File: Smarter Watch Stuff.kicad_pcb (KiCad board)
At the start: 2 copper layers, 39.5 x 39.5 mm, 63 parts, among them J3 CX70M-24P1, M1 Motor_DC, Q1 2N7002, Q2 2N7002, Q3 2N7002, Q4 2N7002, SW1 SW_SPST, SW2 SW_SPST, U1 MCP7940N-xSN, U10 MAX30102, U11 BMI160, U12 M24C64-WMN6TP, U2 TSL25911FN, U3 MCP73831-2-MC, U4 TCR2EE10, U5 ESP32-C6-MINI-1, U6 SHTC3, U7 TMP117xxDRV, U9 MIC5365-1.8YC5, Y1 Crystal

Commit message: Layout start
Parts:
- added C15: 1nF, Capacitor_SMD:C_0603_1608Metric, F.Cu at (100.5, 83.4)
- added C16: 4.7uF, Capacitor_SMD:C_0402_1005Metric, F.Cu at (106.9, 83.2)
- added C17: 100pF, Capacitor_SMD:C_0603_1608Metric, F.Cu at (100.5, 86.0)
- added C18: 2.2uF, Capacitor_SMD:C_0603_1608Metric, F.Cu at (100.5, 88.5)
- added C19: 100pF, Capacitor_SMD:C_0603_1608Metric, F.Cu at (100.5, 91.0)
- added R21: 470R, Resistor_SMD:R_0402_1005Metric, F.Cu at (104.0, 83.2)
- added R22: 470R, Resistor_SMD:R_0402_1005Metric, F.Cu at (104.0, 85.2)
- added R23: 470R, Resistor_SMD:R_0402_1005Metric, F.Cu at (104.0, 87.2)
- added U13: ~, Package_DFN_QFN:DFN-12-1EP_3x3mm_P0.5mm_EP1.6x2.5mm, F.Cu at (49.1, 79.1)
- SW1, SW2: moved to B.Cu
- moved U11 111.5 mm to (49.8, 71.2), turned to 180 degrees
- moved C14 103.9 mm to (54.0, 68.0)
- moved Y1 101.6 mm to (35.0, 70.5), turned to 90 degrees
- moved U1 97.0 mm to (41.0, 71.0)
- moved U12 96.8 mm to (45.0, 90.5)
- moved J6 96.7 mm to (39.0, 90.5)
- moved J5 95.8 mm to (36.5, 90.5)
- moved J4 94.8 mm to (34.0, 90.5)
- moved J2 79.4 mm to (51.0, 90.5)
- moved J1 74.1 mm to (53.5, 90.5)
- moved U3 73.8 mm to (36.9, 96.8)
- moved U6 62.2 mm to (49.9, 67.0)
- moved SW2 29.9 mm to (67.5, 65.5), turned to 180 degrees
- moved SW1 29.7 mm to (67.5, 62.0), turned to 180 degrees
- moved D2 9.39 mm to (36.5, 63.6)

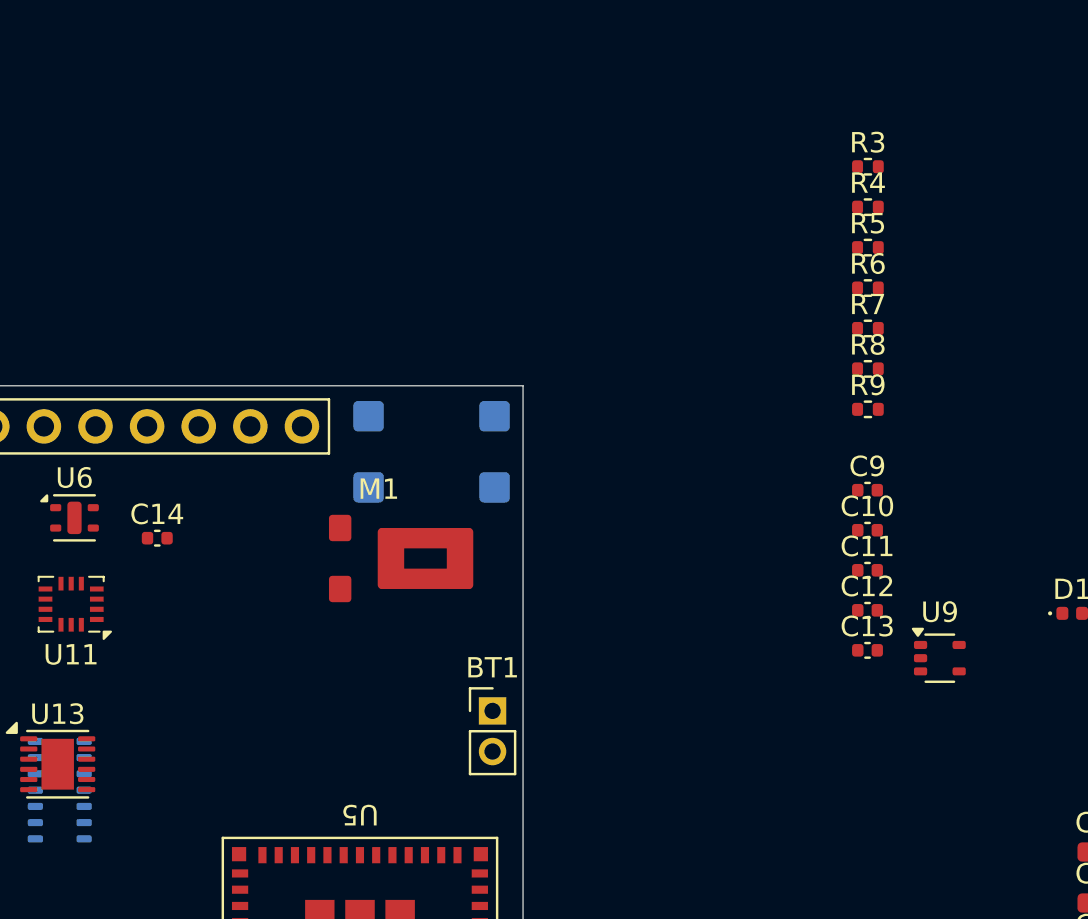
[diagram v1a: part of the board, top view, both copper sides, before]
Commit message: added one r and c and ldo to heart rate ting
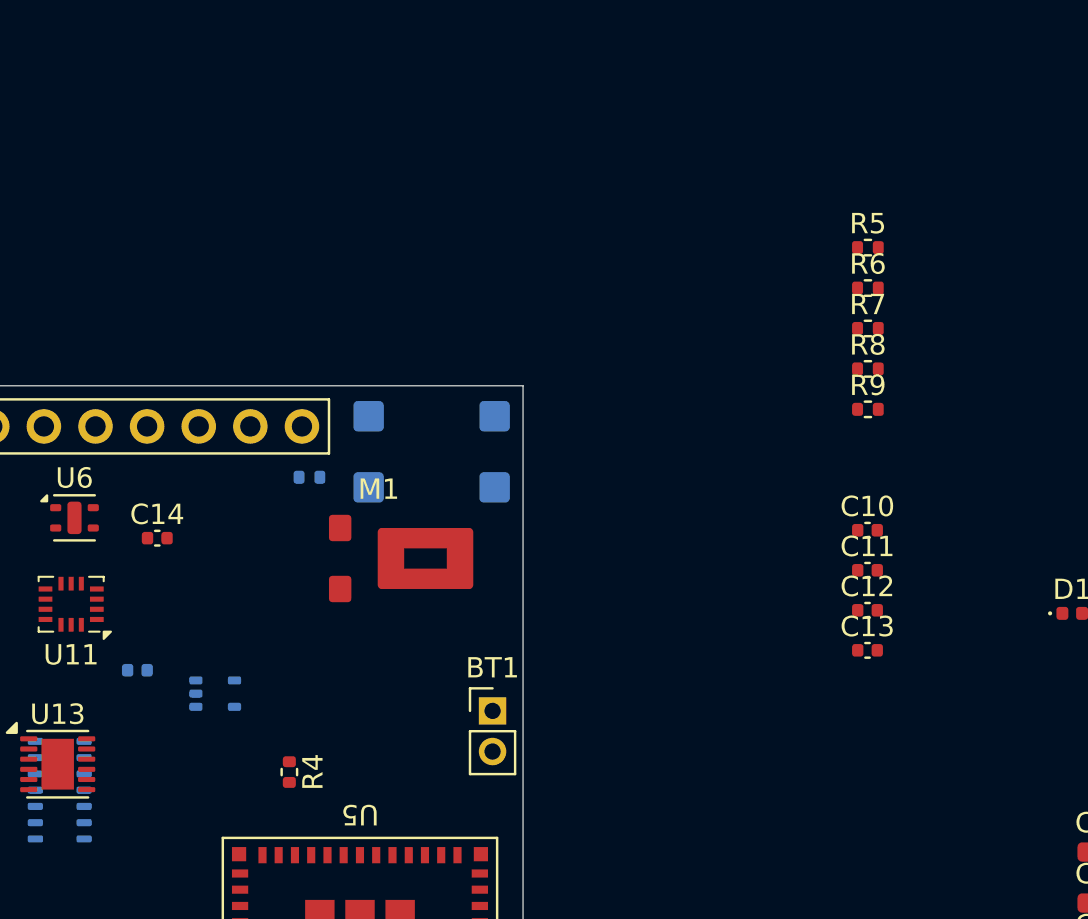
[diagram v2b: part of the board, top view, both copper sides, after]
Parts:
- C9, R3, U9: moved to B.Cu
- moved R4 39.8 mm to (60.5, 79.5), turned to -90 degrees
- moved C9 37.0 mm to (53.0, 74.5), turned to 180 degrees
- moved U9 35.7 mm to (56.9, 75.7)
- moved R3 31.4 mm to (61.5, 65.0), turned to 180 degrees
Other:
- copper layers 2 -> 4

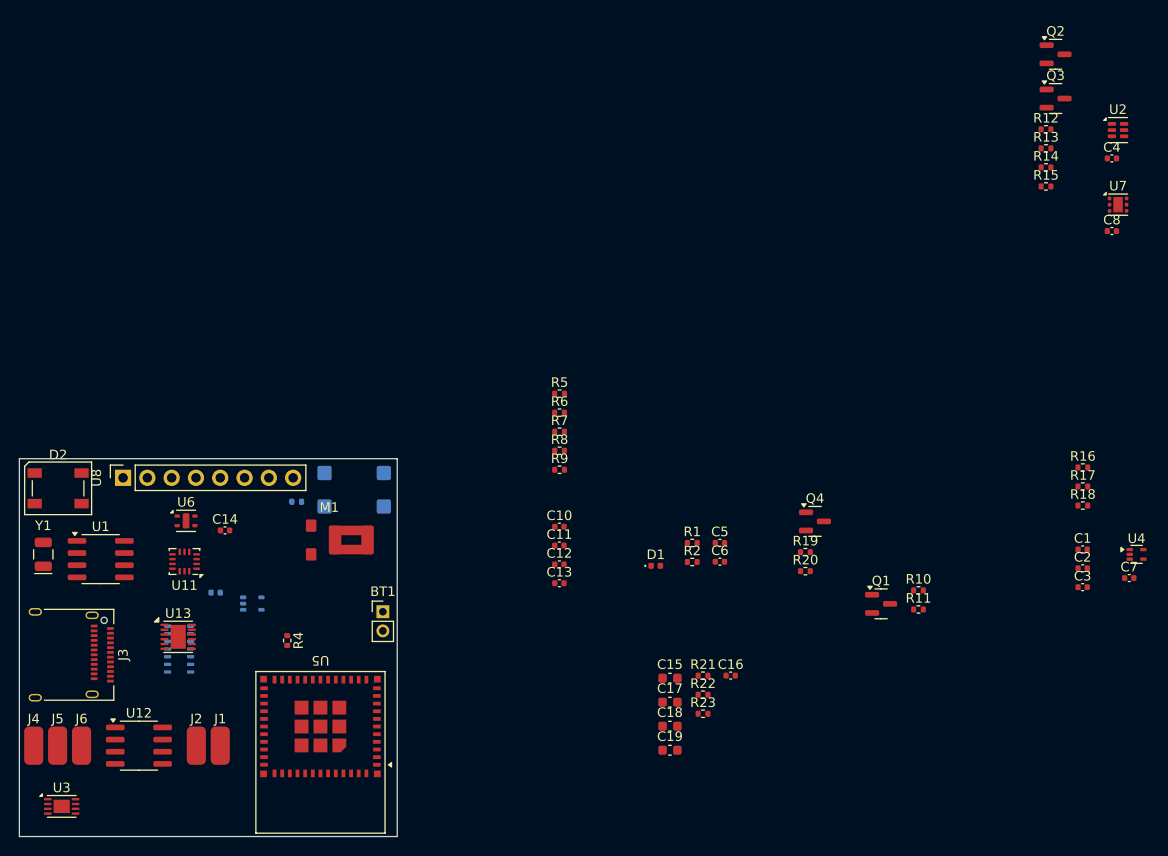
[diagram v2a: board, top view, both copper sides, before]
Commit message: Layout progress
Added logo, moved resistors, etc.
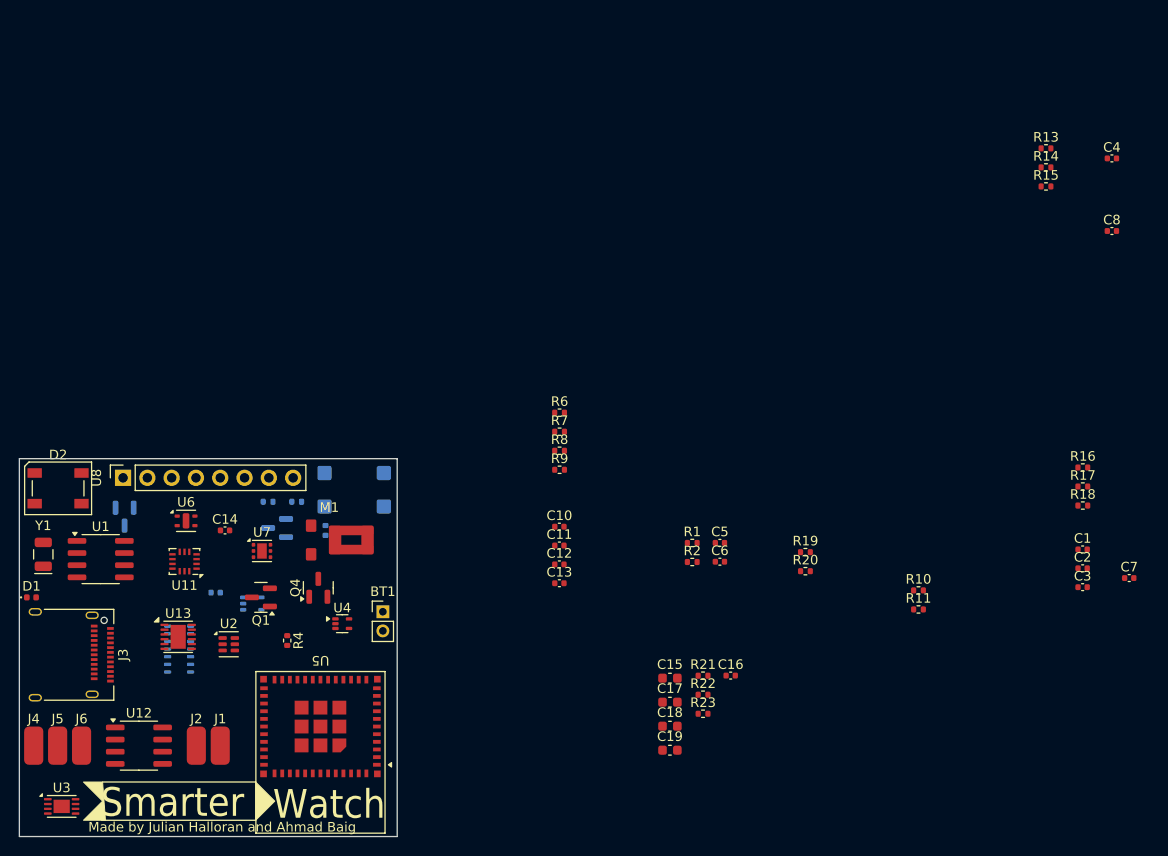
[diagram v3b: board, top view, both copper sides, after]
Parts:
- Q2, Q3, R12, R5: moved to B.Cu
- moved Q2 108.7 mm to (43.5, 66.6), turned to -90 degrees
- moved U2 107.4 mm to (54.4, 79.9)
- moved U7 96.5 mm to (57.9, 70.2)
- moved Q3 92.9 mm to (59.4, 67.8), turned to 180 degrees
- moved R12 90.2 mm to (58.5, 65.0)
- moved U4 83.4 mm to (66.2, 77.8)
- moved D1 65.3 mm to (33.8, 75.0)
- moved Q1 64.8 mm to (57.8, 75.0), turned to 180 degrees
- moved Q4 52.4 mm to (63.8, 74.0), turned to 90 degrees
- moved R5 28.3 mm to (64.5, 68.0), turned to -90 degrees
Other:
- board text added: "Made by Julian Halloran and Ahmad Baig"
- board text added: "Smarter"
- board text added: "Watch"

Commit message: layout progress
added various resistors to layout
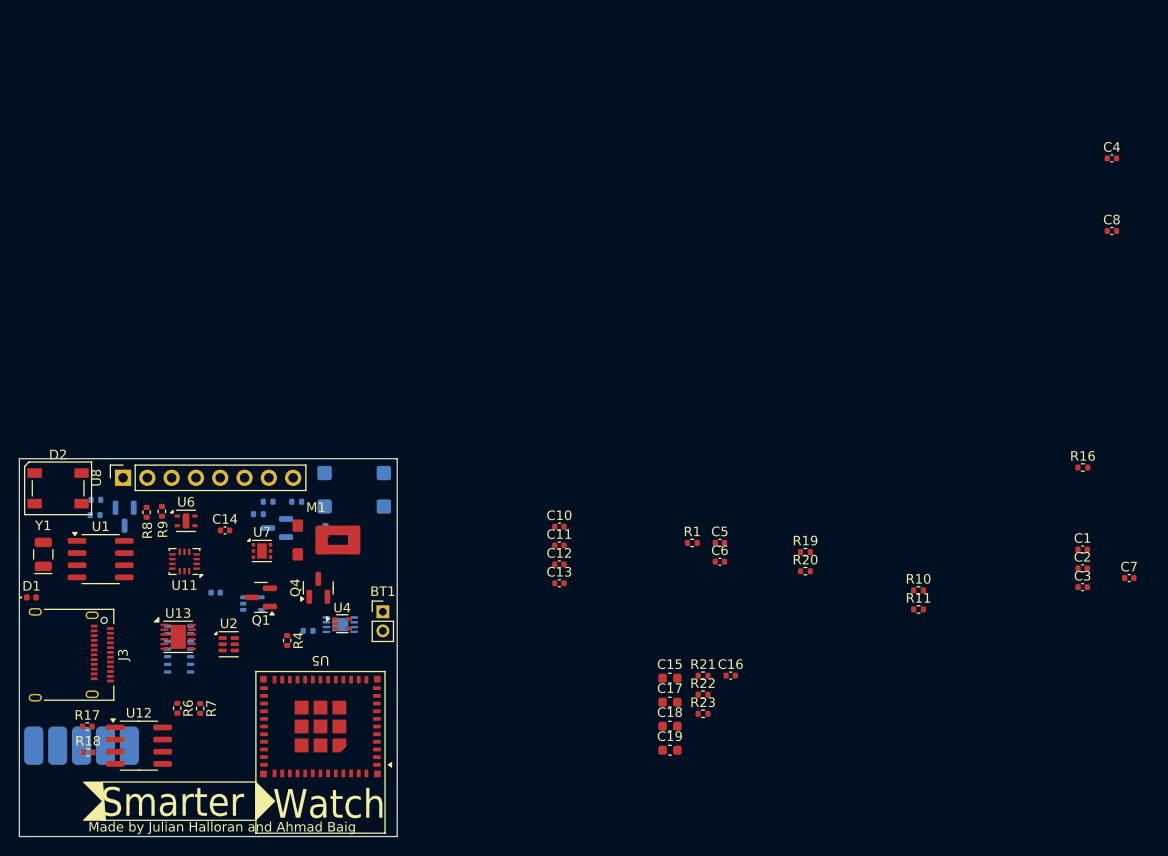
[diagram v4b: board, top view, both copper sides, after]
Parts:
- J1, J2, J4, J5, J6, R13, R14, R15, R2, U3: moved to B.Cu
- moved R18 107.1 mm to (39.7, 91.2)
- moved R17 107.1 mm to (39.6, 88.5)
- moved R13 105.9 mm to (40.5, 64.8)
- moved R15 105.2 mm to (40.4, 66.4), turned to 180 degrees
- moved R14 90.0 mm to (57.5, 66.3)
- moved R6 50.5 mm to (49.0, 86.6), turned to -90 degrees
- moved R7 47.4 mm to (51.4, 86.6), turned to -90 degrees
- moved R8 43.7 mm to (45.8, 66.1), turned to 90 degrees
- moved R9 41.8 mm to (47.4, 66.0), turned to 90 degrees
- moved R2 40.8 mm to (62.7, 78.5)
- moved U3 34.8 mm to (66.0, 77.8), turned to 180 degrees
- moved J1 12.0 mm to (41.5, 90.5), turned to 180 degrees
- moved J2 7.00 mm to (44.0, 90.5), turned to 180 degrees
- moved J4 5.00 mm to (39.0, 90.5), turned to 180 degrees
- moved J6 5.00 mm to (34.0, 90.5), turned to 180 degrees
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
